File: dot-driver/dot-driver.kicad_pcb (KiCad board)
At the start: 2 copper layers, 33 x 41.3 mm, 60 parts, among them J1 5VL, J10 Conn_01x03_Male, J11 Conn_01x03_Male, J12 Conn_01x03_Male, J13 Conn_01x03_Male, J14 Micro_SD_Card_Det_Hirose_DM3AT, J15 SWD, J2 5VL, J3 GND, J4 GND, J5 USB_B_Micro, J6 Conn_01x03_Male, J7 Conn_01x03_Male, J8 Conn_01x03_Male, J9 Conn_01x03_Male, SW1 BUTTON, U1 AP2127N-3.3, U2 STM32F105RCTx, Y1 12MHz

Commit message: Add gerbers
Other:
- board text added: "8ch driver rev 1 by Eric Van Albert"
- board text added: "Rainbow Vomit"
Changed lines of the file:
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@@
   (general
     (thickness 1.6)
-    (drawings 36)
+    (drawings 38)
     (tracks 461)
     (zones 0)
@@
       (outputformat 1)
       (mirror false)
-      (drillshape 1)
+      (drillshape 0)
       (scaleselection 1)
-      (outputdirectory ""))
+      (outputdirectory "gerber/"))
   )
   (net 0 "")
@@
     )
   )
+  (gr_text "8ch driver\nrev 1\nby Eric Van Albert" (at 154.305 94.615 90) (layer B.SilkS)
+    (effects (font (size 0.7 0.7) (thickness 0.15)) (justify mirror))
+  )
+  (gr_text "Rainbow Vomit" (at 151.765 94.615 90) (layer B.SilkS)
+    (effects (font (size 1 1) (thickness 0.2)) (justify mirror))
+  )
   (gr_text GND (at 130.048 116.967) (layer B.SilkS)

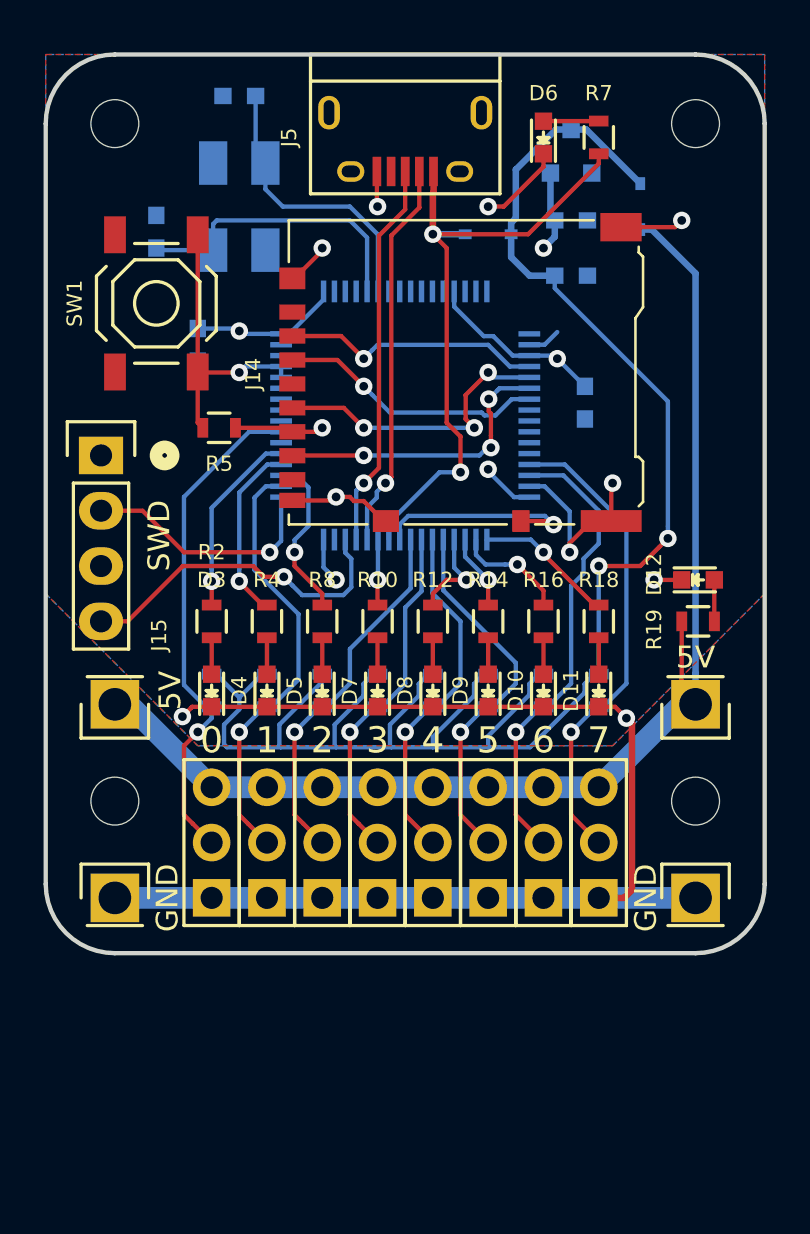
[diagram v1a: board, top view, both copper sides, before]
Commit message: Improve schematic and layout, but they are out of sync
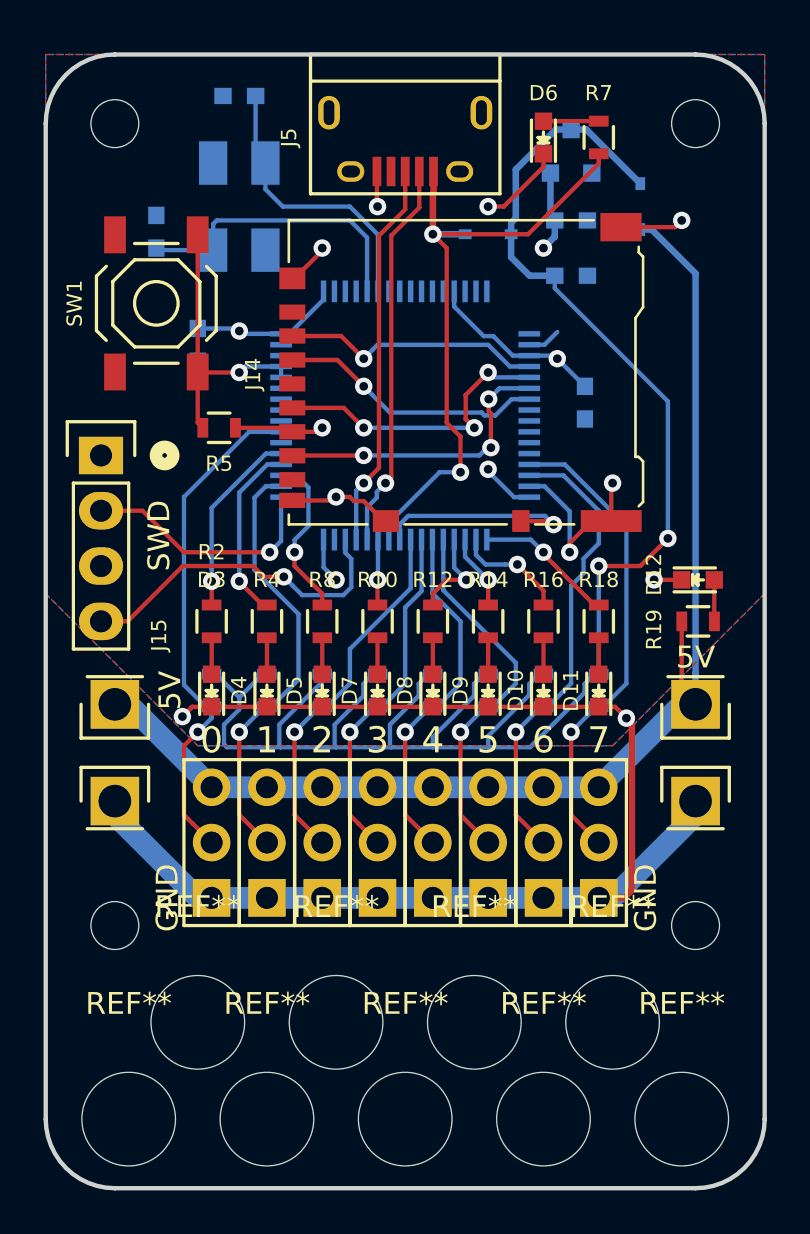
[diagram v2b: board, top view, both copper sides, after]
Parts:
- added REF**: MountingHole_4.3mm_M4, Mounting_Holes:MountingHole_4.3mm_M4, F.Cu at (150.5, 121.3)
- added REF**: MountingHole_4.3mm_M4, Mounting_Holes:MountingHole_4.3mm_M4, F.Cu at (137.8, 121.3)
- added REF**: MountingHole_4.3mm_M4, Mounting_Holes:MountingHole_4.3mm_M4, F.Cu at (131.4, 121.3)
- added REF**: MountingHole_4.3mm_M4, Mounting_Holes:MountingHole_4.3mm_M4, F.Cu at (144.1, 121.3)
- added REF**: MountingHole_4.3mm_M4, Mounting_Holes:MountingHole_4.3mm_M4, F.Cu at (153.7, 125.7)
- added REF**: MountingHole_4.3mm_M4, Mounting_Holes:MountingHole_4.3mm_M4, F.Cu at (147.3, 125.7)
- added REF**: MountingHole_4.3mm_M4, Mounting_Holes:MountingHole_4.3mm_M4, F.Cu at (141.0, 125.7)
- added REF**: MountingHole_4.3mm_M4, Mounting_Holes:MountingHole_4.3mm_M4, F.Cu at (134.6, 125.7)
- added REF**: MountingHole_4.3mm_M4, Mounting_Holes:MountingHole_4.3mm_M4, F.Cu at (128.3, 125.7)
- moved REF** 5.72 mm to (127.6, 116.8)
- moved REF** 5.72 mm to (154.3, 116.8)
- moved J3 4.44 mm to (127.6, 111.1)
- moved J4 4.44 mm to (154.3, 111.1)
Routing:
- net GND: track 86.8 -> 92.5 mm
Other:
- board size 33 x 41.3 mm -> 33 x 52.1 mm

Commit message: Route rev2 of driver board
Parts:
- removed D10, D11: YELLOW, LEDs:LED_0603
- removed D12: GREEN, LEDs:LED_0603
- removed the D3 at (132.1, 106.0)
- removed the J14 at (143.5, 91.4)
- removed the R1 at (132.1, 106.0)
- removed R10, R12, R14, R16, R18, R4, R8: 470R, Resistors_SMD:R_0603
- removed R11, R13, R15, R17, R3, R6, R9: 1K, Resistors_SMD:R_0603
- removed R19, R7: 680R, Resistors_SMD:R_0603
- removed the REF** at (153.7, 125.7)
- removed the REF** at (147.3, 125.7)
- removed the REF** at (141.0, 125.7)
- removed the REF** at (134.6, 125.7)
- removed the REF** at (128.3, 125.7)
- added D5: GREEN, LEDs:LED_0603, F.Cu at (148.3, 78.9)
- added J15: Micro_SD_Card_Det_Hirose_DM3AT, Connector_Card:microSD_HC_Hirose_DM3AT-SF-PEJM5, F.Cu at (143.5, 91.4)
- added J5: External button, Pin_Headers:Pin_Header_Straight_1x02, F.Cu at (131.4, 92.1)
- added Q1: SSM3J338R, TO_SOT_Packages_SMD:SOT-23, B.Cu at (149.0, 80.4)
- added REF**: MountingHole_4.3mm_M4, Mounting_Holes:MountingHole_4.3mm_M4, F.Cu at (153.7, 123.2)
- added REF**: MountingHole_4.3mm_M4, Mounting_Holes:MountingHole_4.3mm_M4, F.Cu at (147.3, 123.2)
- added REF**: MountingHole_4.3mm_M4, Mounting_Holes:MountingHole_4.3mm_M4, F.Cu at (141.0, 123.2)
- added REF**: MountingHole_4.3mm_M4, Mounting_Holes:MountingHole_4.3mm_M4, F.Cu at (134.6, 123.2)
- added REF**: MountingHole_4.3mm_M4, Mounting_Holes:MountingHole_4.3mm_M4, F.Cu at (128.3, 123.2)
- added RN1: 480R, Resistors_SMD:R_Array_Convex_5x0603, B.Cu at (132.2, 102.6)
- added RN2: 1K, Resistors_SMD:R_Array_Convex_5x0603, B.Cu at (149.8, 102.6)
- D1, D2: value D -> YELLOW; footprint Diodes_SMD:SOD-323 -> LEDs:LED_0603; moved to F.Cu
- D6: value GREEN -> YELLOW
- J11: renamed from J1; value 5VL -> 5V
- J12: renamed from J2; value 5VL -> 5V
- R1: renamed from R5; moved to B.Cu
- R2: value 470R -> 680R
- Y1: value 12MHz -> 8MHz
- moved D1 27.8 mm to (132.1, 103.4), turned to 90 degrees
- moved R2 26.9 mm to (148.3, 81.4), turned to 0 degrees
- moved D6 23.3 mm to (142.2, 103.4)
- moved D2 21.0 mm to (134.6, 103.5), turned to 90 degrees
- moved R1 6.51 mm to (129.3, 88.3), turned to 270 degrees
- moved D7 5.73 mm to (144.8, 103.4)
- moved D9 5.73 mm to (149.9, 103.4)
- moved D4 5.73 mm to (139.7, 103.4)
- moved D8 5.68 mm to (147.3, 103.5)
- moved U1 5.45 mm to (144.6, 85.0)
- moved C4 3.93 mm to (149.1, 88.9), turned to 0 degrees
- moved J16 3.24 mm to (127.6, 92.1)
- moved J11 3.18 mm to (127.6, 103.5)
- moved J12 3.18 mm to (154.3, 103.5)
- moved J1 3.17 mm to (132.1, 112.4)
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- renumbered C5 to C3, C6 to C4, C3 to C5, C4 to C6, D5 to D3, J6 to J1, J13 to J10, J3 to J13, J4 to J14, J15 to J16, J5 to J2, J7 to J3, J8 to J4, J9 to J6, J10 to J7, J11 to J8, J12 to J9
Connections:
- D1 pad 1: +5V -> /INDCAT0
- D1 pad 2: +5VL -> /IND0
- D2 pad 1: +5V -> /INDCAT1
- D2 pad 2: /VBUS -> /IND1
- D3 pad 1: GND -> /INDCAT2
- D3 pad 2: Net-(D5-Pad2) -> /IND2
- D4 pad 1: GND -> /INDCAT3
- D4 pad 2: Net-(D4-Pad2) -> /IND3
- D6 pad 1: GND -> /INDCAT4
- D6 pad 2: Net-(D6-Pad2) -> /IND4
- D7 pad 1: GND -> /INDCAT5
- D7 pad 2: Net-(D7-Pad2) -> /IND5
- D8 pad 1: GND -> /INDCAT6
- D8 pad 2: Net-(D8-Pad2) -> /IND6
- D9 pad 1: GND -> /INDCAT7
- D9 pad 2: Net-(D9-Pad2) -> /IND7
- J1 pad 3: +5VL -> +5V
- J10 pad 3: +5VL -> +5V
- J11 pad 1: +5VL -> +5V
- J12 pad 1: +5VL -> +5V
- J3 pad 3: +5VL -> +5V
- J4 pad 3: +5VL -> +5V
- J6 pad 3: +5VL -> +5V
- J7 pad 3: +5VL -> +5V
- J8 pad 3: +5VL -> +5V
- J9 pad 3: +5VL -> +5V
- R2 pad 1: Net-(D3-Pad2) -> +5V
- R2 pad 2: /IND0 -> Net-(D5-Pad2)
- U2 pad 20: /NSS -> Net-(U2-Pad20)
- U2 pad 21: /SCK -> Net-(U2-Pad21)
- U2 pad 22: /MISO -> Net-(U2-Pad22)
- U2 pad 23: /MOSI -> /DETECT
- U2 pad 26: Net-(U2-Pad26) -> /IND7
- U2 pad 27: Net-(U2-Pad27) -> /IND5
- U2 pad 28: Net-(U2-Pad28) -> /IND6
- U2 pad 33: /IND7 -> /NSS
- U2 pad 34: /IND6 -> /SCK
- U2 pad 35: /IND5 -> /MISO
- U2 pad 36: /IND4 -> /MOSI
- U2 pad 41: /DETECT -> Net-(U2-Pad41)
- U2 pad 51: /IND2 -> /IND1
- U2 pad 52: /IND1 -> /IND2
- U2 pad 53: /IND0 -> Net-(U2-Pad53)
- U2 pad 56: Net-(U2-Pad56) -> /IND0
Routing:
- net +5VL: track 57.1 -> 0.00 mm
- net /INDCAT7: track 0.00 -> 29.2 mm, vias 0 -> 1
- net GND: track 92.5 -> 65.6 mm, vias 11 -> 10
- net /INDCAT6: track 0.00 -> 21.8 mm, vias 0 -> 1
- net /LED0: track 23.3 -> 42.2 mm
- net /INDCAT5: track 0.00 -> 17.4 mm, vias 0 -> 1
- net /LED1: track 20.0 -> 37.4 mm
- net /INDCAT4: track 0.00 -> 14.1 mm, vias 0 -> 1
- net /LED2: track 16.9 -> 29.5 mm
- net /IND5: track 3.44 -> 11.8 mm
- net /INDCAT3: track 0.00 -> 8.28 mm, vias 0 -> 1
- net +5V: track 83.6 -> 75.6 mm, vias 2 -> 1
- net /INDCAT2: track 0.00 -> 7.06 mm, vias 0 -> 1
- net /LED3: track 16.1 -> 22.8 mm
- net /BUTTON: track 13.7 -> 19.9 mm, vias 1 -> 2
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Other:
- board size 33 x 52.1 mm -> 33 x 49.5 mm
- board text added: "8ch driver rev 2 by Eric Van Albert"
- board text removed: "8ch driver rev 1 by Eric Van Albert"

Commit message: Generate rev2 gerbers
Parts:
- R2: moved to B.Cu
- moved R2 2.43 mm to (148.6, 79.0)
- moved Q1 1.38 mm to (148.6, 81.7), turned to 270 degrees
- moved SW1 0.64 mm to (129.5, 86.4)
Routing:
- net /VBUS: track 29.3 -> 26.0 mm
- net /BUTTON: track 19.9 -> 20.9 mm
- net /INDCAT7: track 29.2 -> 29.9 mm
- net +5V: track 75.6 -> 76.1 mm, vias 1 -> 0
- net Net-(D5-Pad2): track 2.54 -> 2.86 mm, vias 0 -> 1
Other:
- board text added: "BUTTON"
- board text added: "Rainbow Vomit 8ch driver rev 2 by Eric Van Albert"
- board text removed: "8ch driver rev 2 by Eric Van Albert"
- board text removed: "Rainbow Vomit"

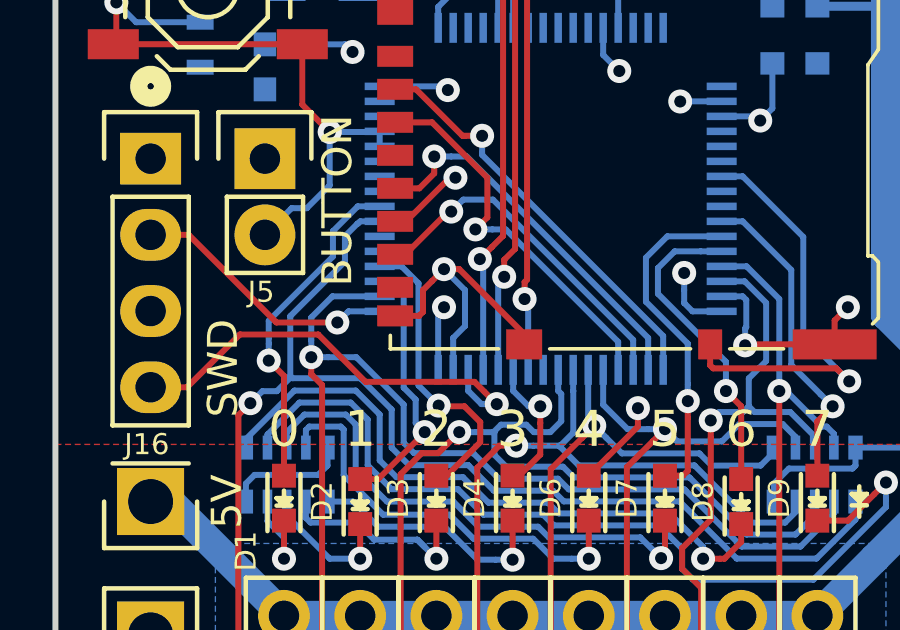
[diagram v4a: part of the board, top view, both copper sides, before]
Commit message: Begin work on static pattern for firefly
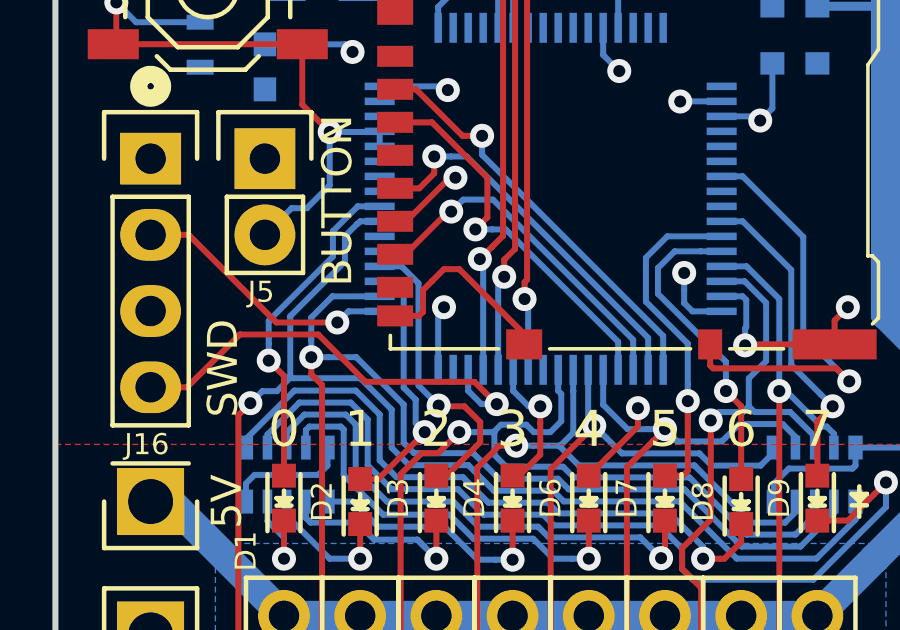
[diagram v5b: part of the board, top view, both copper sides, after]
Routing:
- net GND: track 65.3 -> 61.5 mm, vias 10 -> 9
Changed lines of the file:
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@@
     (thickness 1.6)
     (drawings 56)
-    (tracks 586)
+    (tracks 581)
     (zones 0)
     (modules 53)
@@
   (layers
     (0 F.Cu signal hide)
-    (31 B.Cu signal hide)
+    (31 B.Cu signal)
     (32 B.Adhes user)
     (33 F.Adhes user)
@@
     (37 F.SilkS user hide)
     (38 B.Mask user)
-    (39 F.Mask user)
+    (39 F.Mask user hide)
     (40 Dwgs.User user)
     (41 Cmts.User user)
@@
     (pad_to_mask_clearance 0.2)
     (aux_axis_origin 0 0)
-    (visible_elements FFFD7F7F)
+    (visible_elements FFFDFF7F)
     (pcbplotparams
       (layerselection 0x010fc_ffffffff)
@@
   (segment (start 142.72 87.715) (end 142.72 88.618) (width 0.2) (layer B.Cu) (net 1))
   (segment (start 142.72 88.618) (end 143.256 89.154) (width 0.2) (layer B.Cu) (net 1))
-  (via (at 137.414 95.758) (size 0.8) (drill 0.4) (layers F.Cu B.Cu) (net 1))
   (segment (start 135.785 97.315) (end 136.585 97.315) (width 0.2) (layer F.Cu) (net 1))
   (segment (start 136.713998 97.186002) (end 136.713998 96.458002) (width 0.2) (layer F.Cu) (net 1))
@@
   (segment (start 136.713998 96.458002) (end 137.014001 96.157999) (width 0.2) (layer F.Cu) (net 1))
   (segment (start 136.585 97.315) (end 136.713998 97.186002) (width 0.2) (layer F.Cu) (net 1))
-  (segment (start 137.72 98.049698) (end 137.72 99.115) (width 0.2) (layer B.Cu) (net 1))
-  (segment (start 138.114001 97.655697) (end 137.72 98.049698) (width 0.2) (layer B.Cu) (net 1))
-  (segment (start 137.414 95.758) (end 138.114001 96.458001) (width 0.2) (layer B.Cu) (net 1))
-  (segment (start 138.114001 96.458001) (end 138.114001 97.655697) (width 0.2) (layer B.Cu) (net 1))
   (segment (start 133.53 102.305) (end 133.219 102.616) (width 0.2) (layer B.Cu) (net 1))
   (segment (start 133.53 101.705) (end 133.53 102.305) (width 0.2) (layer B.Cu) (net 1))
